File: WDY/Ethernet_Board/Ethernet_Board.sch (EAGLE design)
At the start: 35 parts, among them J1 22-05-7028-02, J2 22-05-7108-10, P1 RB1-125BAG1A, T1 EXMACHINA-LOGO-NAME, X1 ASE_50

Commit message: Re-size the board
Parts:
- MP1, MP2, MP3, MP4: value MOUNT-PAD3,0 -> MOUNT-HOLE3.0; device holes:MOUNT-PAD3,0 -> holes:MOUNT-HOLE3.0
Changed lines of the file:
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@@
 <part name="JP3" library="SparkFun" deviceset="FIDUCIAL" device="1X2" value="FIDUCIAL1X2"/>
 <part name="JP4" library="SparkFun" deviceset="FIDUCIAL" device="1X2" value="FIDUCIAL1X2"/>
-<part name="MP4" library="holes" deviceset="MOUNT-PAD" device="3,0"/>
-<part name="MP3" library="holes" deviceset="MOUNT-PAD" device="3,0"/>
-<part name="MP2" library="holes" deviceset="MOUNT-PAD" device="3,0"/>
-<part name="MP1" library="holes" deviceset="MOUNT-PAD" device="3,0"/>
+<part name="MP4" library="holes" deviceset="MOUNT-HOLE" device="3.0"/>
+<part name="MP3" library="holes" deviceset="MOUNT-HOLE" device="3.0"/>
+<part name="MP2" library="holes" deviceset="MOUNT-HOLE" device="3.0"/>
+<part name="MP1" library="holes" deviceset="MOUNT-HOLE" device="3.0"/>
 <part name="R8" library="rcl" deviceset="R-EU_" device="R0603" value="2K2"/>
 <part name="J2" library="con-molex" deviceset="22-?-10" device="05-7108"/>
@@
 <instance part="JP3" gate="G$1" x="352.298" y="21.59"/>
 <instance part="JP4" gate="G$1" x="356.362" y="21.59"/>
-<instance part="MP4" gate="1" x="248.92" y="10.16"/>
-<instance part="MP3" gate="1" x="233.68" y="10.16"/>
-<instance part="MP2" gate="1" x="213.36" y="10.16"/>
-<instance part="MP1" gate="1" x="193.04" y="10.16"/>
+<instance part="MP4" gate="G$1" x="248.92" y="10.16"/>
+<instance part="MP3" gate="G$1" x="233.68" y="10.16"/>
+<instance part="MP2" gate="G$1" x="213.36" y="10.16"/>
+<instance part="MP1" gate="G$1" x="193.04" y="10.16"/>
 <instance part="R8" gate="G$1" x="360.68" y="208.28" rot="R270"/>
 <instance part="J2" gate="-1" x="327.66" y="91.44"/>

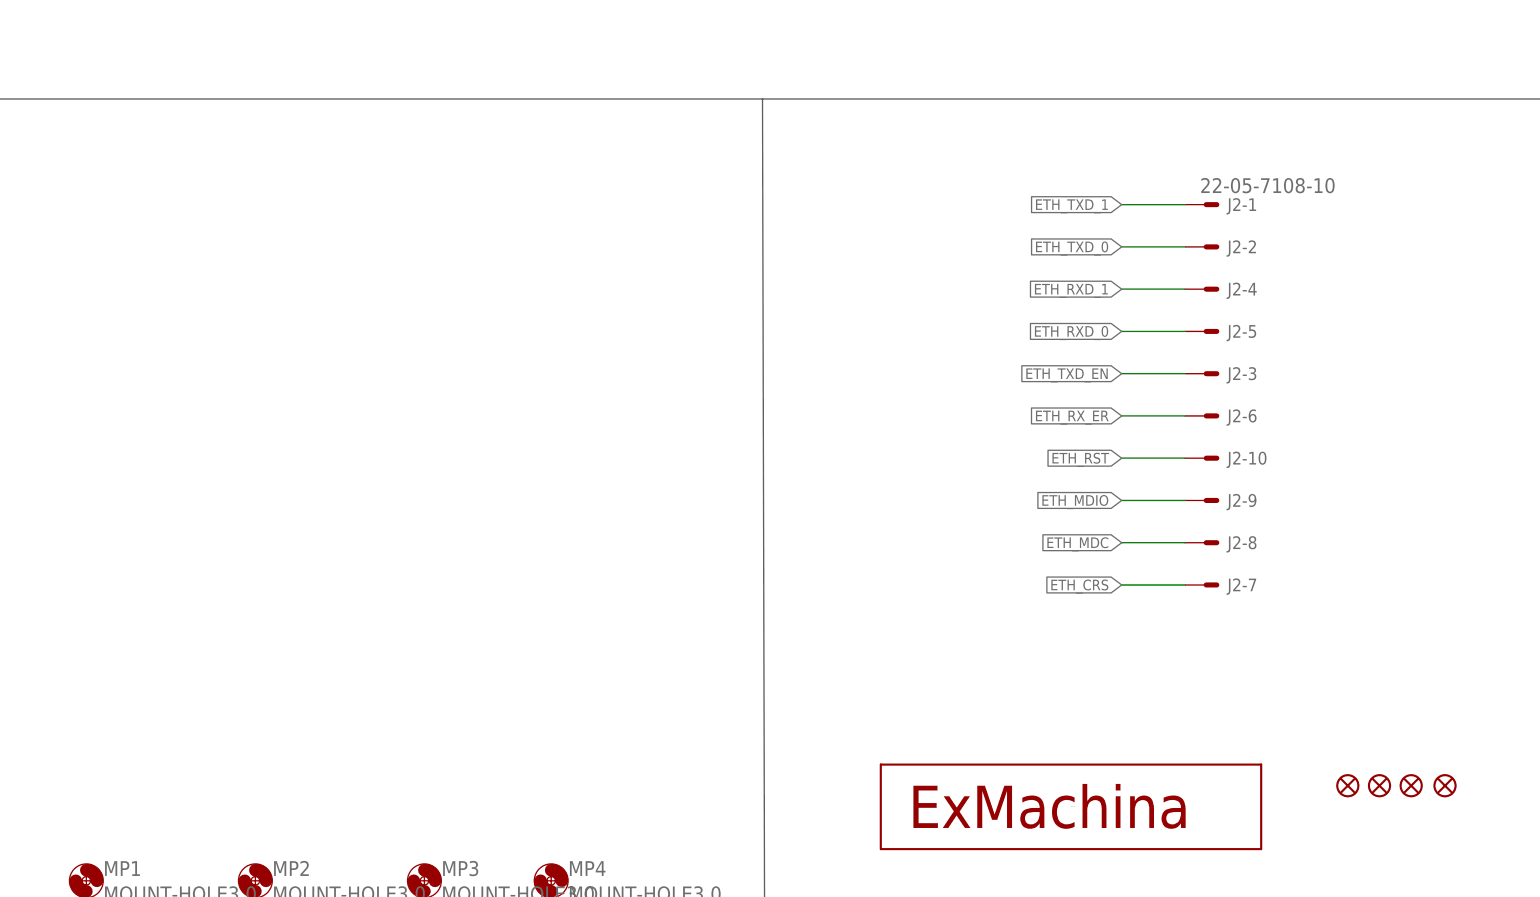
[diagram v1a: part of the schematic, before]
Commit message: Split 12pts connectors on to 2x6pts connectors Adding 50MHz on output connector
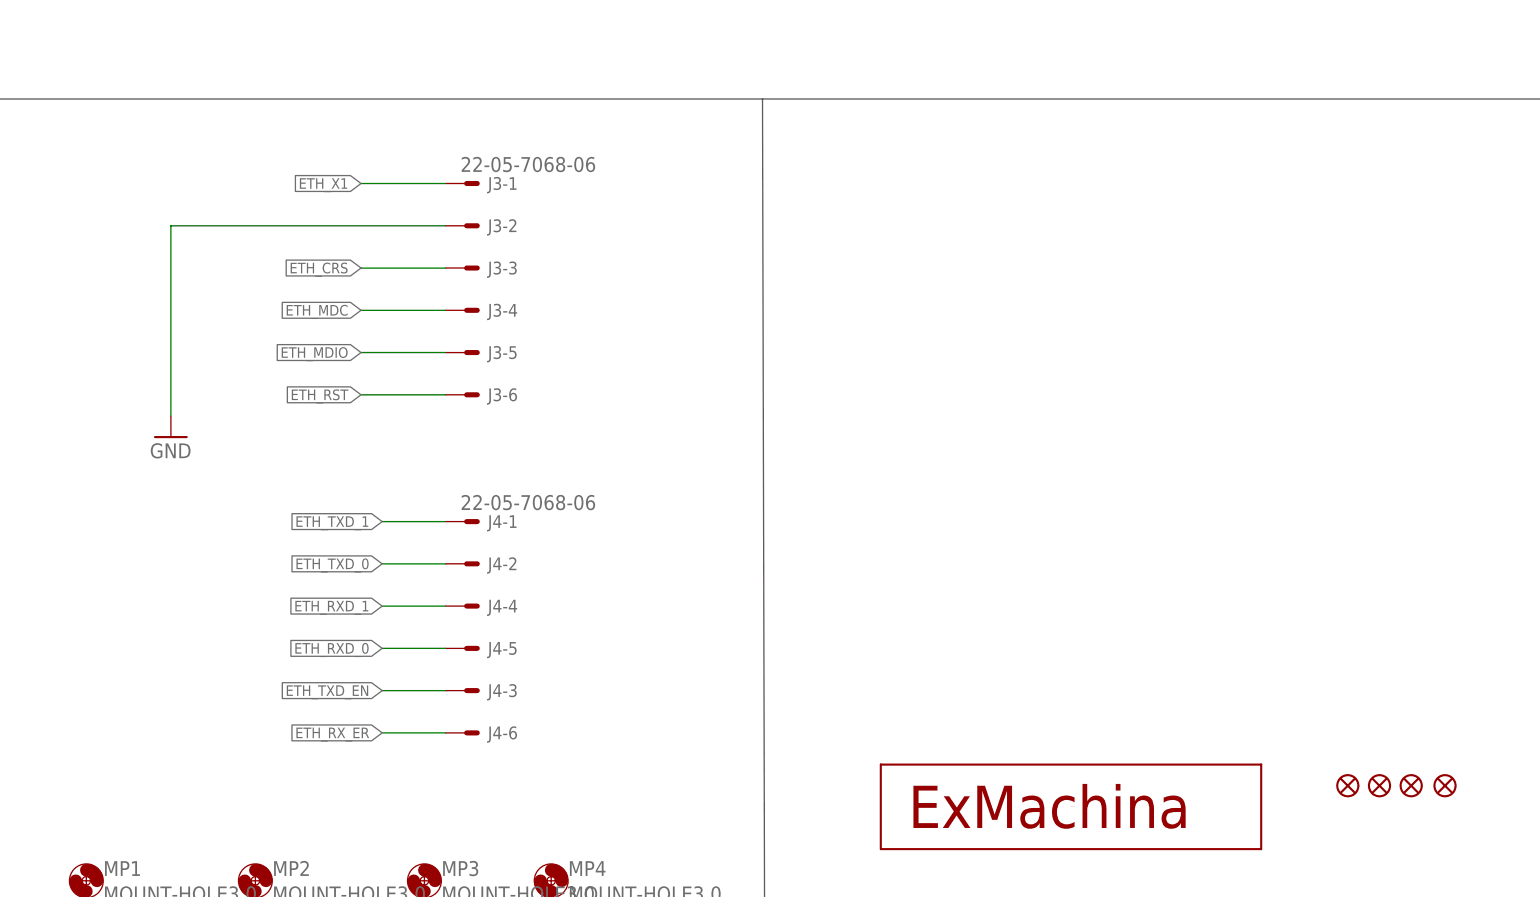
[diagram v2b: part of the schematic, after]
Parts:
- removed J2: 22-05-7108-10, con-molex:22-05-7108-10
- added J3, J4: 22-05-7068-06, con-molex:22-05-7068-06
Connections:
- net ETH_CRS: now also J3-3.S; no longer J2-7.S
- net ETH_MDC: now also J3-4.S; no longer J2-8.S
- net ETH_MDIO: now also J3-5.S; no longer J2-9.S
- net ETH_RST: now also J3-6.S; no longer J2-10.S
- net ETH_RXD_0: now also J4-5.S; no longer J2-5.S
- net ETH_RXD_1: now also J4-4.S; no longer J2-4.S
- net ETH_RX_ER: now also J4-6.S; no longer J2-6.S
- net ETH_TXD_0: now also J4-2.S; no longer J2-2.S
- net ETH_TXD_1: now also J4-1.S; no longer J2-1.S
- net ETH_TXD_EN: now also J4-3.S; no longer J2-3.S
- net ETH_X1: now also J3-1.S
- net GND: now also J3-2.S
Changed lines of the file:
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@@
 <part name="MP1" library="holes" deviceset="MOUNT-HOLE" device="3.0"/>
 <part name="R8" library="rcl" deviceset="R-EU_" device="R0603" value="2K2"/>
-<part name="J2" library="con-molex" deviceset="22-?-10" device="05-7108"/>
 <part name="J1" library="con-molex" deviceset="22-?-02" device="05-7028"/>
 <part name="+3V31" library="supply1" deviceset="+3V3" device=""/>
 <part name="GND1" library="supply1" deviceset="GND" device=""/>
 <part name="D1" library="diode" deviceset="STPS3L40?" device="UF" value="STPS3L40UF"/>
+<part name="J3" library="con-molex" deviceset="22-?-06" device="05-7068"/>
+<part name="J4" library="con-molex" deviceset="22-?-06" device="05-7068"/>
+<part name="GND17" library="supply1" deviceset="GND" device=""/>
 </parts>
 <sheets>
@@
 <instance part="MP1" gate="G$1" x="193.04" y="10.16"/>
 <instance part="R8" gate="G$1" x="360.68" y="208.28" rot="R270"/>
-<instance part="J2" gate="-1" x="327.66" y="91.44"/>
-<instance part="J2" gate="-2" x="327.66" y="86.36"/>
-<instance part="J2" gate="-4" x="327.66" y="81.28"/>
-<instance part="J2" gate="-5" x="327.66" y="76.2"/>
-<instance part="J2" gate="-3" x="327.66" y="71.12"/>
-<instance part="J2" gate="-6" x="327.66" y="66.04"/>
-<instance part="J2" gate="-10" x="327.66" y="60.96"/>
-<instance part="J2" gate="-9" x="327.66" y="55.88"/>
-<instance part="J2" gate="-8" x="327.66" y="50.8"/>
-<instance part="J2" gate="-7" x="327.66" y="45.72"/>
 <instance part="J1" gate="-1" x="27.94" y="76.2" rot="R180"/>
 <instance part="J1" gate="-2" x="27.94" y="81.28" rot="R180"/>
@@
 <instance part="GND1" gate="1" x="40.64" y="60.96"/>
 <instance part="D1" gate="A" x="55.88" y="78.74" rot="R90"/>
+<instance part="J3" gate="-1" x="238.76" y="93.98"/>
+<instance part="J3" gate="-2" x="238.76" y="88.9"/>
+<instance part="J3" gate="-3" x="238.76" y="83.82"/>
+<instance part="J3" gate="-4" x="238.76" y="78.74"/>
+<instance part="J3" gate="-5" x="238.76" y="73.66"/>
+<instance part="J3" gate="-6" x="238.76" y="68.58"/>
+<instance part="J4" gate="-1" x="238.76" y="53.34"/>
+<instance part="J4" gate="-2" x="238.76" y="48.26"/>
+<instance part="J4" gate="-4" x="238.76" y="43.18"/>
+<instance part="J4" gate="-5" x="238.76" y="38.1"/>
+<instance part="J4" gate="-3" x="238.76" y="33.02"/>
+<instance part="J4" gate="-6" x="238.76" y="27.94"/>
+<instance part="GND17" gate="1" x="203.2" y="63.5"/>
 </instances>
 <busses>
@@
 <wire x1="55.88" y1="73.66" x2="40.64" y2="73.66" width="0.1524" layer="91"/>
 <junction x="40.64" y="73.66"/>
+</segment>
+<segment>
+<pinref part="J3" gate="-2" pin="S"/>
+<pinref part="GND17" gate="1" pin="GND"/>
+<wire x1="236.22" y1="88.9" x2="203.2" y2="88.9" width="0.1524" layer="91"/>
+<wire x1="203.2" y1="88.9" x2="203.2" y2="66.04" width="0.1524" layer="91"/>
 </segment>
 </net>
@@
 </segment>
 <segment>
-<wire x1="325.12" y1="71.12" x2="317.5" y2="71.12" width="0.1524" layer="91"/>
-<label x="317.5" y="71.12" size="1.27" layer="95" rot="R180" xref="yes"/>
-<pinref part="J2" gate="-3" pin="S"/>
+<wire x1="236.22" y1="33.02" x2="228.6" y2="33.02" width="0.1524" layer="91"/>
+<label x="228.6" y="33.02" size="1.27" layer="95" rot="R180" xref="yes"/>
+<pinref part="J4" gate="-3" pin="S"/>
 </segment>
 </net>
@@
 </segment>
 <segment>
-<wire x1="325.12" y1="66.04" x2="317.5" y2="66.04" width="0.1524" layer="91"/>
-<label x="317.5" y="66.04" size="1.27" layer="95" rot="R180" xref="yes"/>
-<pinref part="J2" gate="-6" pin="S"/>
+<wire x1="236.22" y1="27.94" x2="228.6" y2="27.94" width="0.1524" layer="91"/>
+<label x="228.6" y="27.94" size="1.27" layer="95" rot="R180" xref="yes"/>
+<pinref part="J4" gate="-6" pin="S"/>
 </segment>
 </net>
@@
 </segment>
 <segment>
-<wire x1="325.12" y1="45.72" x2="317.5" y2="45.72" width="0.1524" layer="91"/>
-<label x="317.5" y="45.72" size="1.27" layer="95" rot="R180" xref="yes"/>
-<pinref part="J2" gate="-7" pin="S"/>
+<wire x1="236.22" y1="83.82" x2="226.06" y2="83.82" width="0.1524" layer="91"/>
+<pinref part="J3" gate="-3" pin="S"/>
+<label x="226.06" y="83.82" size="1.27" layer="95" rot="R180" xref="yes"/>
 </segment>
 </net>
@@
 <label x="337.82" y="190.5" size="1.27" layer="95" xref="yes"/>
 </segment>
+<segment>
+<wire x1="226.06" y1="93.98" x2="236.22" y2="93.98" width="0.1524" layer="91"/>
+<label x="226.06" y="93.98" size="1.27" layer="95" rot="R180" xref="yes"/>
+<pinref part="J3" gate="-1" pin="S"/>
+</segment>
 </net>
 <net name="ETH_MDC" class="1">
@@
 </segment>
 <segment>
-<wire x1="325.12" y1="50.8" x2="317.5" y2="50.8" width="0.1524" layer="91"/>
-<label x="317.5" y="50.8" size="1.27" layer="95" rot="R180" xref="yes"/>
-<pinref part="J2" gate="-8" pin="S"/>
+<wire x1="236.22" y1="78.74" x2="226.06" y2="78.74" width="0.1524" layer="91"/>
+<label x="226.06" y="78.74" size="1.27" layer="95" rot="R180" xref="yes"/>
+<pinref part="J3" gate="-4" pin="S"/>
 </segment>
 </net>
@@
 </segment>
 <segment>
-<wire x1="325.12" y1="55.88" x2="317.5" y2="55.88" width="0.1524" layer="91"/>
-<label x="317.5" y="55.88" size="1.27" layer="95" rot="R180" xref="yes"/>
-<pinref part="J2" gate="-9" pin="S"/>
+<wire x1="236.22" y1="73.66" x2="226.06" y2="73.66" width="0.1524" layer="91"/>
+<pinref part="J3" gate="-5" pin="S"/>
+<label x="226.06" y="73.66" size="1.27" layer="95" rot="R180" xref="yes"/>
 </segment>
 </net>
@@
 </segment>
 <segment>
-<wire x1="325.12" y1="60.96" x2="317.5" y2="60.96" width="0.1524" layer="91"/>
-<label x="317.5" y="60.96" size="1.27" layer="95" rot="R180" xref="yes"/>
-<pinref part="J2" gate="-10" pin="S"/>
+<wire x1="236.22" y1="68.58" x2="226.06" y2="68.58" width="0.1524" layer="91"/>
+<label x="226.06" y="68.58" size="1.27" layer="95" rot="R180" xref="yes"/>
+<pinref part="J3" gate="-6" pin="S"/>
 </segment>
 </net>
@@
 </segment>
 <segment>
-<wire x1="325.12" y1="86.36" x2="317.5" y2="86.36" width="0.1524" layer="91"/>
-<pinref part="J2" gate="-2" pin="S"/>
-<label x="317.5" y="86.36" size="1.27" layer="95" rot="R180" xref="yes"/>
+<wire x1="236.22" y1="48.26" x2="228.6" y2="48.26" width="0.1524" layer="91"/>
+<label x="228.6" y="48.26" size="1.27" layer="95" rot="R180" xref="yes"/>
+<pinref part="J4" gate="-2" pin="S"/>
 </segment>
 </net>
@@
 </segment>
 <segment>
-<wire x1="325.12" y1="91.44" x2="317.5" y2="91.44" width="0.1524" layer="91"/>
-<pinref part="J2" gate="-1" pin="S"/>
-<label x="317.5" y="91.44" size="1.27" layer="95" rot="R180" xref="yes"/>
+<wire x1="236.22" y1="53.34" x2="228.6" y2="53.34" width="0.1524" layer="91"/>
+<label x="228.6" y="53.34" size="1.27" layer="95" rot="R180" xref="yes"/>
+<pinref part="J4" gate="-1" pin="S"/>
 </segment>
 </net>
@@
 </segment>
 <segment>
-<wire x1="325.12" y1="81.28" x2="317.5" y2="81.28" width="0.1524" layer="91"/>
-<pinref part="J2" gate="-4" pin="S"/>
-<label x="317.5" y="81.28" size="1.27" layer="95" rot="R180" xref="yes"/>
+<wire x1="236.22" y1="43.18" x2="228.6" y2="43.18" width="0.1524" layer="91"/>
+<label x="228.6" y="43.18" size="1.27" layer="95" rot="R180" xref="yes"/>
+<pinref part="J4" gate="-4" pin="S"/>
 </segment>
 </net>
@@
 </segment>
 <segment>
-<wire x1="325.12" y1="76.2" x2="317.5" y2="76.2" width="0.1524" layer="91"/>
-<pinref part="J2" gate="-5" pin="S"/>
-<label x="317.5" y="76.2" size="1.27" layer="95" rot="R180" xref="yes"/>
-</segment>
-</net>
+<wire x1="236.22" y1="38.1" x2="228.6" y2="38.1" width="0.1524" layer="91"/>
+<label x="228.6" y="38.1" size="1.27" layer="95" rot="R180" xref="yes"/>
+<pinref part="J4" gate="-5" pin="S"/>
+</segment>
+</net>

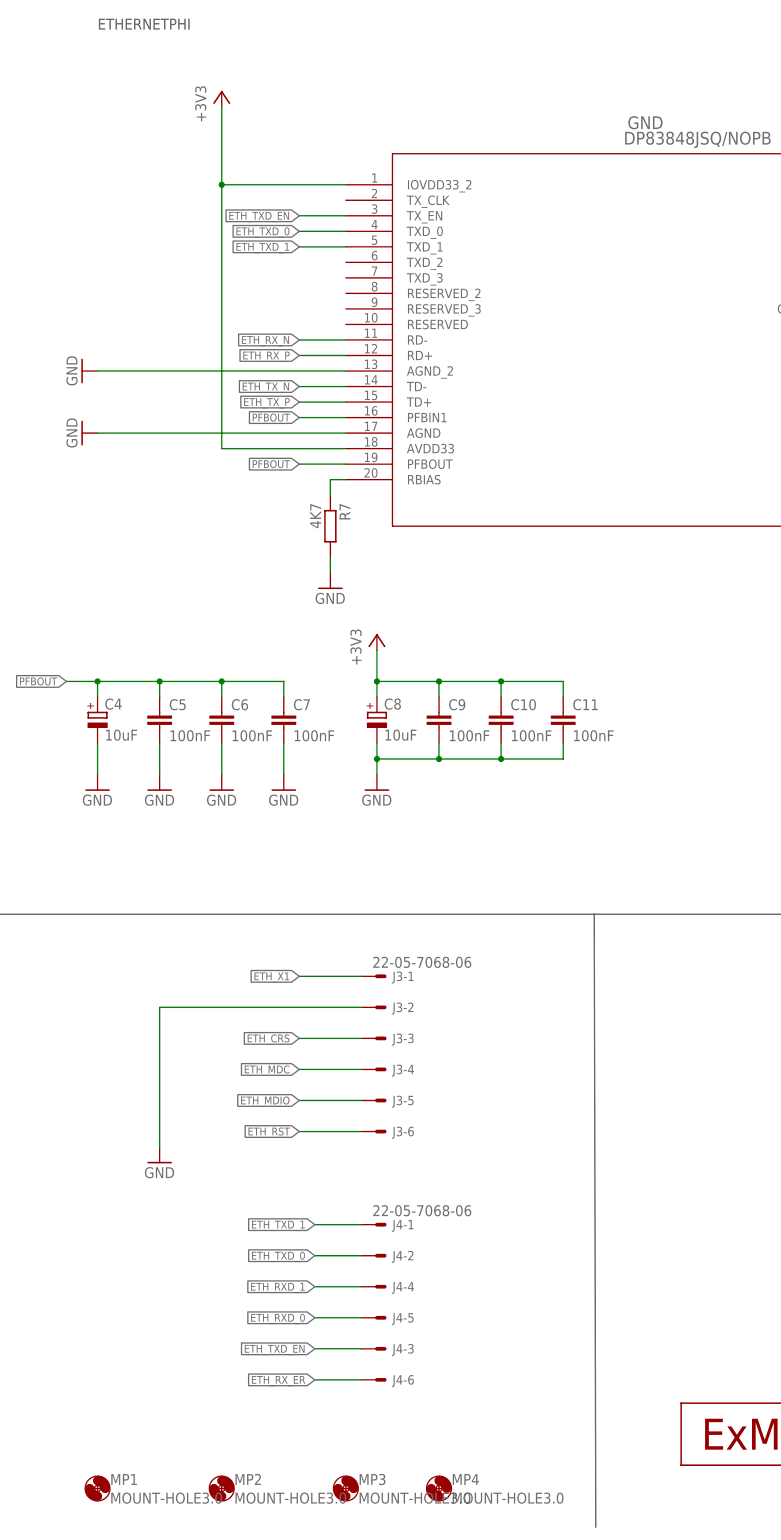
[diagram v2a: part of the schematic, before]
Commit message: Renumber part and add 4mm fillet
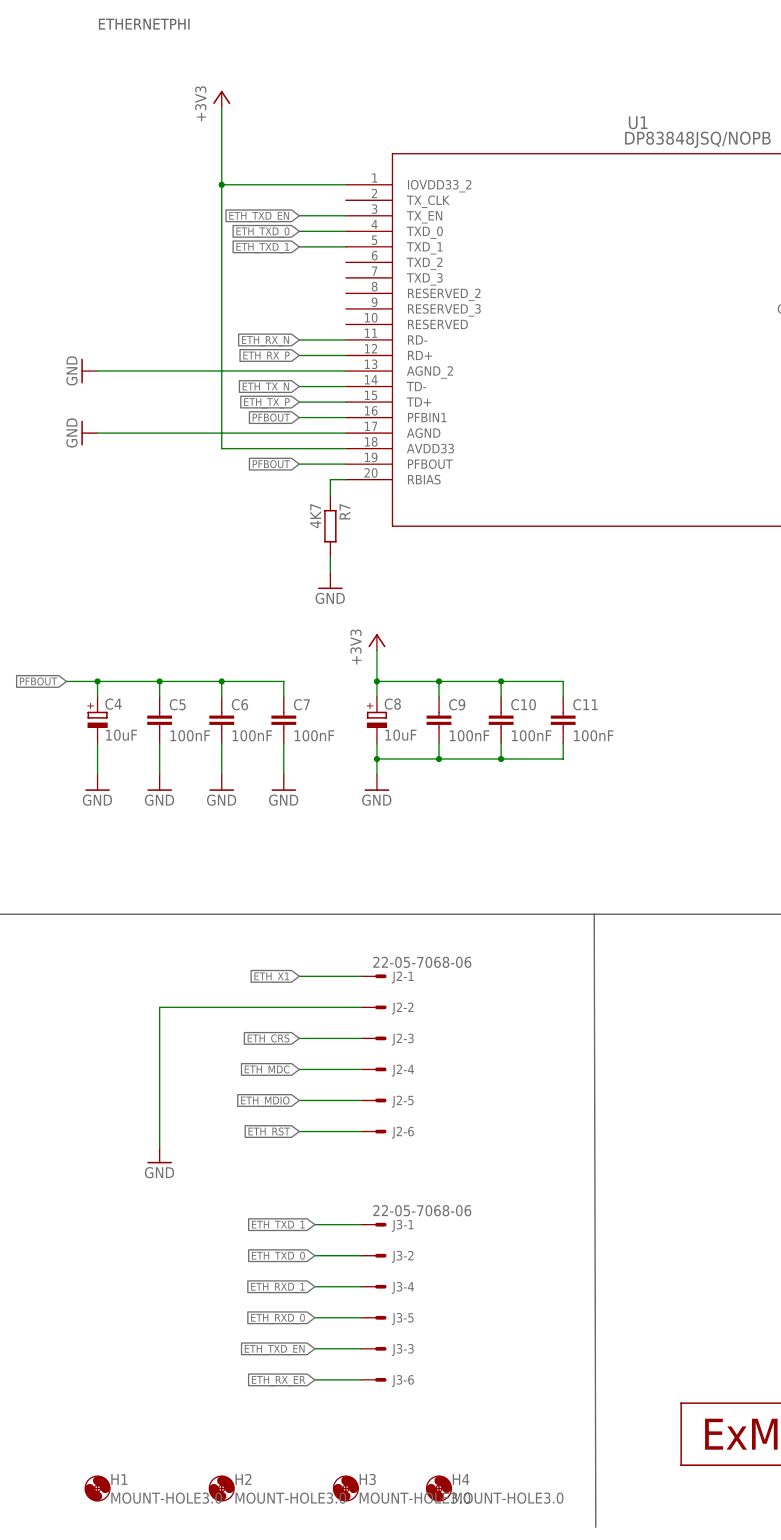
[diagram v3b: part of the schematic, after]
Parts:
- removed J4: 22-05-7068-06, con-molex:22-05-7068-06
- added J2: 22-05-7068-06, con-molex:22-05-7068-06
- renumbered GND to U1, MP1 to H1, MP2 to H2, MP3 to H3, MP4 to H4
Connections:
- net ETH_CRS: now also J2-3.S; no longer J3-3.S
- net ETH_MDC: now also J2-4.S; no longer J3-4.S
- net ETH_MDIO: now also J2-5.S; no longer J3-5.S
- net ETH_RST: now also J2-6.S; no longer J3-6.S
- net ETH_RXD_0: now also J3-5.S; no longer J4-5.S
- net ETH_RXD_1: now also J3-4.S; no longer J4-4.S
- net ETH_RX_ER: now also J3-6.S; no longer J4-6.S
- net ETH_TXD_0: now also J3-2.S; no longer J4-2.S
- net ETH_TXD_1: now also J3-1.S; no longer J4-1.S
- net ETH_TXD_EN: now also J3-3.S; no longer J4-3.S
- net ETH_X1: now also J2-1.S; no longer J3-1.S
- net GND: now also J2-2.S; no longer J3-2.S
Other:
- moved on the sheet: J3-1, J3-2, J3-3, J3-4, J3-5, J3-6
